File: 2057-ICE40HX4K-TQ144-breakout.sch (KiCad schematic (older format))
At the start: 41 parts, among them J1 Conn_02x30_Odd_Even, J2 Conn_02x30_Odd_Even, J3 RaspberryPI-B+header, J4 0548190519, J5 RaspberryPI-B+header, J6 Conn_02x06_Odd_Even, J7 Conn_02x01, U1 ICE40HX4K-TQ144, U2 AZ1117CH-3.3TRG1, U3 AZ1117CH-1.2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

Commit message: Added some ground vias, schematic PDF & some digikey nos.
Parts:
- C18, C20: Digi-Key_PN 1276-6455-1-ND -> 1276-1119-1-ND; MPN (none) -> CL10A106MQ8NNNC
- C19, C21: Digi-Key_PN 1276-6780-1-ND -> 1276-2868-1-ND; MPN (none) -> CL10A226MQ8NRNE
- C3, C5: Digi-Key_PN (none) -> 1276-1119-1-ND; MPN (none) -> CL10A106MQ8NNNC
- U1: Digi-Key_PN (none) -> 220-1572-ND; MPN (none) -> ICE40HX4K-TQ144
- U2: MPN (none) -> AZ1117CH-3.3TRG1
- U3: MPN (none) -> AZ1117CH-1.2TRG1
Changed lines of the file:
@@
 F 2 "Package_QFP:TQFP-144_20x20mm_P0.5mm" H 3100 1000 50  0001 R CNN
 F 3 "http://www.latticesemi.com/Products/FPGAandCPLD/iCE40" H 1100 5400 50  0001 C CNN
+F 4 "220-1572-ND" H 2100 2900 50  0001 C CNN "Digi-Key_PN"
+F 5 "ICE40HX4K-TQ144" H 2100 2900 50  0001 C CNN "MPN"
 	1    2100 2900
 	1    0    0    -1
@@
 F 2 "Package_QFP:TQFP-144_20x20mm_P0.5mm" H 5150 900 50  0001 R CNN
 F 3 "http://www.latticesemi.com/Products/FPGAandCPLD/iCE40" H 3150 5300 50  0001 C CNN
+F 4 "220-1572-ND" H 4150 2800 50  0001 C CNN "Digi-Key_PN"
+F 5 "ICE40HX4K-TQ144" H 4150 2800 50  0001 C CNN "MPN"
 	2    4150 2800
 	1    0    0    -1
@@
 F 2 "Package_QFP:TQFP-144_20x20mm_P0.5mm" H 8700 1400 50  0001 R CNN
 F 3 "http://www.latticesemi.com/Products/FPGAandCPLD/iCE40" H 6700 5800 50  0001 C CNN
+F 4 "220-1572-ND" H 7700 3300 50  0001 C CNN "Digi-Key_PN"
+F 5 "ICE40HX4K-TQ144" H 7700 3300 50  0001 C CNN "MPN"
 	3    7700 3300
 	1    0    0    -1
@@
 F 2 "Package_QFP:TQFP-144_20x20mm_P0.5mm" H 7050 900 50  0001 R CNN
 F 3 "http://www.latticesemi.com/Products/FPGAandCPLD/iCE40" H 5050 5300 50  0001 C CNN
+F 4 "220-1572-ND" H 6050 2800 50  0001 C CNN "Digi-Key_PN"
+F 5 "ICE40HX4K-TQ144" H 6050 2800 50  0001 C CNN "MPN"
 	4    6050 2800
 	1    0    0    -1
@@
 F 2 "Package_QFP:TQFP-144_20x20mm_P0.5mm" H 11150 850 50  0001 R CNN
 F 3 "http://www.latticesemi.com/Products/FPGAandCPLD/iCE40" H 9150 5250 50  0001 C CNN
+F 4 "220-1572-ND" H 10150 2750 50  0001 C CNN "Digi-Key_PN"
+F 5 "ICE40HX4K-TQ144" H 10150 2750 50  0001 C CNN "MPN"
 	5    10150 2750
 	1    0    0    -1
@@
 F 2 "Capacitor_SMD:C_0603_1608Metric_Pad1.05x0.95mm_HandSolder" H 12138 2050 50  0001 C CNN
 F 3 "~" H 12100 2200 50  0001 C CNN
+F 4 "1276-1119-1-ND" H 12100 2200 50  0001 C CNN "Digi-Key_PN"
+F 5 "CL10A106MQ8NNNC" H 12100 2200 50  0001 C CNN "MPN"
 	1    12100 2200
 	1    0    0    -1
@@
 F 2 "Capacitor_SMD:C_0603_1608Metric_Pad1.05x0.95mm_HandSolder" H 12138 1500 50  0001 C CNN
 F 3 "~" H 12100 1650 50  0001 C CNN
+F 4 "1276-1119-1-ND" H 12100 1650 50  0001 C CNN "Digi-Key_PN"
+F 5 "CL10A106MQ8NNNC" H 12100 1650 50  0001 C CNN "MPN"
 	1    12100 1650
 	1    0    0    -1
@@
 F 3 "https://www.diodes.com/assets/Datasheets/AZ1117.pdf" H 14850 1800 50  0001 C CNN
 F 4 "AZ1117CH-3.3TRG1DICT-ND" H 14850 1800 50  0001 C CNN "Digi-Key_PN"
+F 5 "AZ1117CH-3.3TRG1" H 14850 1800 50  0001 C CNN "MPN"
 	1    14850 1800
 	1    0    0    -1
@@
 F 2 "Capacitor_SMD:C_0603_1608Metric_Pad1.05x0.95mm_HandSolder" H 14288 1800 50  0001 C CNN
 F 3 "~" H 14250 1950 50  0001 C CNN
-F 4 "1276-6455-1-ND" H 14250 1950 50  0001 C CNN "Digi-Key_PN"
+F 4 "1276-1119-1-ND" H 14250 1950 50  0001 C CNN "Digi-Key_PN"
+F 5 "CL10A106MQ8NNNC" H 14250 1950 50  0001 C CNN "MPN"
 	1    14250 1950
 	1    0    0    -1
@@
 F 2 "Capacitor_SMD:C_0603_1608Metric_Pad1.05x0.95mm_HandSolder" H 15338 1800 50  0001 C CNN
 F 3 "~" H 15300 1950 50  0001 C CNN
-F 4 "1276-6780-1-ND" H 15300 1950 50  0001 C CNN "Digi-Key_PN"
+F 4 "1276-2868-1-ND" H 15300 1950 50  0001 C CNN "Digi-Key_PN"
+F 5 "CL10A226MQ8NRNE" H 15300 1950 50  0001 C CNN "MPN"
 	1    15300 1950
 	1    0    0    -1
@@
 F 3 "https://www.diodes.com/assets/Datasheets/AZ1117.pdf" H 14900 2650 50  0001 C CNN
 F 4 "AZ1117CH-1.2TRG1DICT-ND" H 14900 2650 50  0001 C CNN "Digi-Key_PN"
+F 5 "AZ1117CH-1.2TRG1" H 14900 2650 50  0001 C CNN "MPN"
 	1    14900 2650
 	1    0    0    -1
@@
 F 2 "Capacitor_SMD:C_0603_1608Metric_Pad1.05x0.95mm_HandSolder" H 14338 2650 50  0001 C CNN
 F 3 "~" H 14300 2800 50  0001 C CNN
-F 4 "1276-6455-1-ND" H 14300 2800 50  0001 C CNN "Digi-Key_PN"
+F 4 "1276-1119-1-ND" H 14300 2800 50  0001 C CNN "Digi-Key_PN"
+F 5 "CL10A106MQ8NNNC" H 14300 2800 50  0001 C CNN "MPN"
 	1    14300 2800
 	1    0    0    -1
@@
 F 2 "Capacitor_SMD:C_0603_1608Metric_Pad1.05x0.95mm_HandSolder" H 15388 2650 50  0001 C CNN
 F 3 "~" H 15350 2800 50  0001 C CNN
-F 4 "1276-6780-1-ND" H 15350 2800 50  0001 C CNN "Digi-Key_PN"
+F 4 "1276-2868-1-ND" H 15350 2800 50  0001 C CNN "Digi-Key_PN"
+F 5 "CL10A226MQ8NRNE" H 15350 2800 50  0001 C CNN "MPN"
 	1    15350 2800
 	1    0    0    -1

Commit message: Fix programming headers, add LEDs, cosmetic fixes.
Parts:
- removed J6: Conn_02x06_Odd_Even, Connector_PinHeader_2.54mm:PinHeader_2x06_P2.54mm_Vertical, symbol Connector_Generic:Conn_02x06_Odd_Even
- added D10, D2, D3, D4, D5, D6, D7, D8, D9: LED_ALT, LED_SMD:LED_0603_1608Metric_Pad1.05x0.95mm_HandSolder, symbol Device:LED_ALT
- added J6: Conn_02x07_Odd_Even, Connector_PinHeader_2.54mm:PinHeader_2x07_P2.54mm_Vertical, symbol Connector_Generic:Conn_02x07_Odd_Even
- added R10, R11, R12, R13, R14, R6, R7, R8, R9: 330, Resistor_SMD:R_0603_1608Metric_Pad1.05x0.95mm_HandSolder, symbol Device:R
- Y1: footprint digikey-footprints:Oscillator_XLH536025.000000I -> jb-footprint:Oscillator_XLH536025.000000I
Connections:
- wire segments 464 -> 503
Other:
- moved on the sheet: C10, C11, C12, C13, C14, C15, C16, C17, C22, C23, C6, C7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

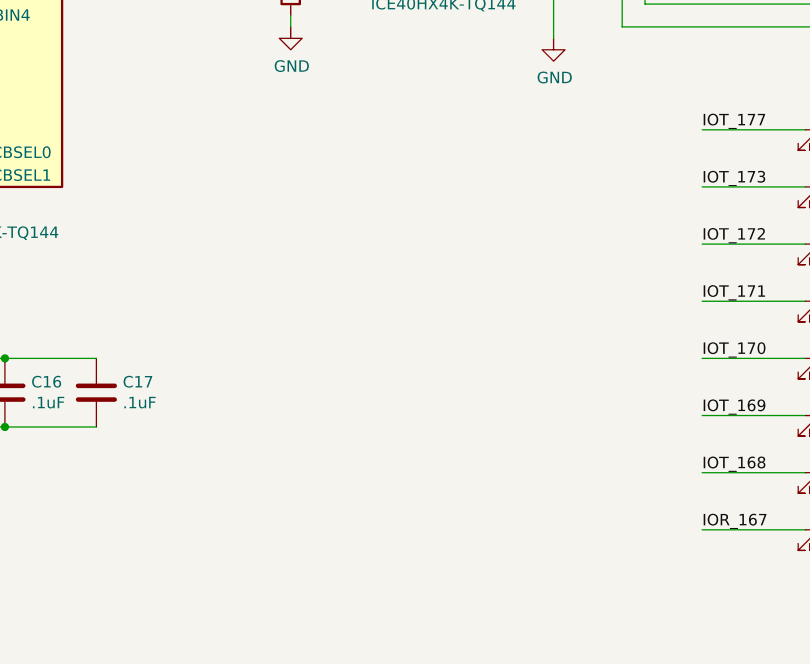
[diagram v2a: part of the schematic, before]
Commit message: Added two pushbuttons.
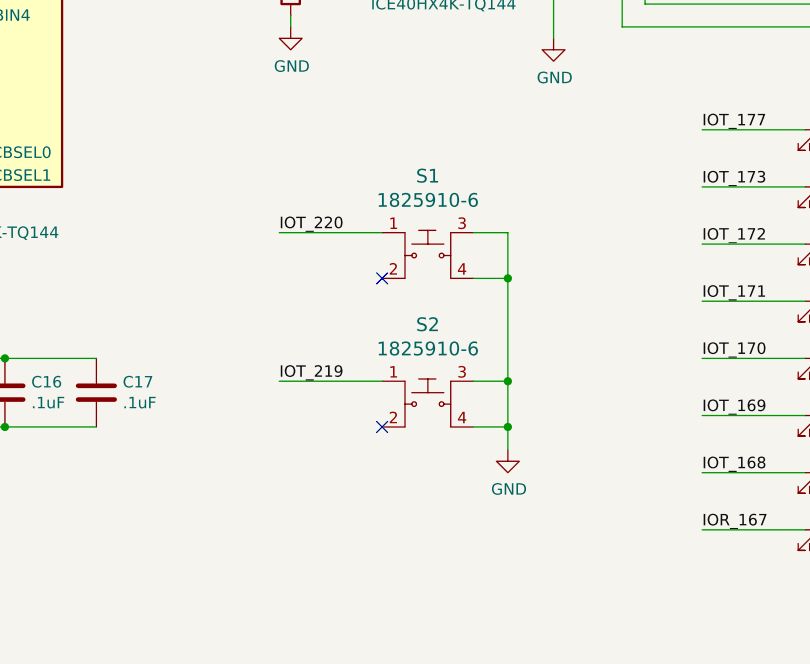
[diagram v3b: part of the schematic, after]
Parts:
- added S1, S2: 1825910-6, digikey-footprints:Switch_Tactile_THT_6x6mm, symbol dk_Tactile-Switches:1825910-6
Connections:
- net GND: now also S1.3, S1.4, S2.3, S2.4
- net IOT_219: now also S2.1
- net IOT_220: now also S1.1
- no-connect marks 5 -> 7
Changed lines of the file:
@@
 Text Label 10800 5850 0    50   ~ 0
 IOR_167
+$Comp
+L dk_Tactile-Switches:1825910-6 S1
+U 1 1 5E33EB87
+P 9600 4650
+F 0 "S1" H 9600 4997 60  0000 C CNN
+F 1 "1825910-6" H 9600 4891 60  0000 C CNN
+F 2 "digikey-footprints:Switch_Tactile_THT_6x6mm" H 9800 4850 60  0001 L CNN
+F 3 "https://www.te.com/commerce/DocumentDelivery/DDEController?Action=srchrtrv&DocNm=1825910&DocType=Customer+Drawing&DocLang=English" H 9800 4950 60  0001 L CNN
+F 4 "450-1650-ND" H 9800 5050 60  0001 L CNN "Digi-Key_PN"
+F 5 "1825910-6" H 9800 5150 60  0001 L CNN "MPN"
+F 6 "Switches" H 9800 5250 60  0001 L CNN "Category"
+F 7 "Tactile Switches" H 9800 5350 60  0001 L CNN "Family"
+F 8 "https://www.te.com/commerce/DocumentDelivery/DDEController?Action=srchrtrv&DocNm=1825910&DocType=Customer+Drawing&DocLang=English" H 9800 5450 60  0001 L CNN "DK_Datasheet_Link"
+F 9 "/product-detail/en/te-connectivity-alcoswitch-switches/1825910-6/450-1650-ND/1632536" H 9800 5550 60  0001 L CNN "DK_Detail_Page"
+F 10 "SWITCH TACTILE SPST-NO 0.05A 24V" H 9800 5650 60  0001 L CNN "Description"
+F 11 "TE Connectivity ALCOSWITCH Switches" H 9800 5750 60  0001 L CNN "Manufacturer"
+F 12 "Active" H 9800 5850 60  0001 L CNN "Status"
+	1    9600 4650
+	1    0    0    -1
+$EndComp
+$Comp
+L dk_Tactile-Switches:1825910-6 S2
+U 1 1 5E3405E8
+P 9600 5300
+F 0 "S2" H 9600 5647 60  0000 C CNN
+F 1 "1825910-6" H 9600 5541 60  0000 C CNN
+F 2 "digikey-footprints:Switch_Tactile_THT_6x6mm" H 9800 5500 60  0001 L CNN
+F 3 "https://www.te.com/commerce/DocumentDelivery/DDEController?Action=srchrtrv&DocNm=1825910&DocType=Customer+Drawing&DocLang=English" H 9800 5600 60  0001 L CNN
+F 4 "450-1650-ND" H 9800 5700 60  0001 L CNN "Digi-Key_PN"
+F 5 "1825910-6" H 9800 5800 60  0001 L CNN "MPN"
+F 6 "Switches" H 9800 5900 60  0001 L CNN "Category"
+F 7 "Tactile Switches" H 9800 6000 60  0001 L CNN "Family"
+F 8 "https://www.te.com/commerce/DocumentDelivery/DDEController?Action=srchrtrv&DocNm=1825910&DocType=Customer+Drawing&DocLang=English" H 9800 6100 60  0001 L CNN "DK_Datasheet_Link"
+F 9 "/product-detail/en/te-connectivity-alcoswitch-switches/1825910-6/450-1650-ND/1632536" H 9800 6200 60  0001 L CNN "DK_Detail_Page"
+F 10 "SWITCH TACTILE SPST-NO 0.05A 24V" H 9800 6300 60  0001 L CNN "Description"
+F 11 "TE Connectivity ALCOSWITCH Switches" H 9800 6400 60  0001 L CNN "Manufacturer"
+F 12 "Active" H 9800 6500 60  0001 L CNN "Status"
+	1    9600 5300
+	1    0    0    -1
+$EndComp
+$Comp
+L power:GND #PWR06
+U 1 1 5E341682
+P 9950 5500
+F 0 "#PWR06" H 9950 5250 50  0001 C CNN
+F 1 "GND" H 9955 5327 50  0000 C CNN
+F 2 "" H 9950 5500 50  0001 C CNN
+F 3 "" H 9950 5500 50  0001 C CNN
+	1    9950 5500
+	1    0    0    -1
+$EndComp
+Wire Wire Line
+	9800 4550 9950 4550
+Wire Wire Line
+	9950 4550 9950 4750
+Wire Wire Line
+	9800 5200 9950 5200
+Connection ~ 9950 5200
+Wire Wire Line
+	9950 5200 9950 5400
+Wire Wire Line
+	9800 5400 9950 5400
+Connection ~ 9950 5400
+Wire Wire Line
+	9950 5400 9950 5500
+Wire Wire Line
+	9800 4750 9950 4750
+Connection ~ 9950 4750
+Wire Wire Line
+	9950 4750 9950 5200
+Wire Wire Line
+	8950 4550 9400 4550
+Wire Wire Line
+	8950 5200 9400 5200
+NoConn ~ 9400 4750
+NoConn ~ 9400 5400
+Text Label 8950 4550 0    50   ~ 0
+IOT_220
+Text Label 8950 5200 0    50   ~ 0
+IOT_219
 $EndSCHEMATC

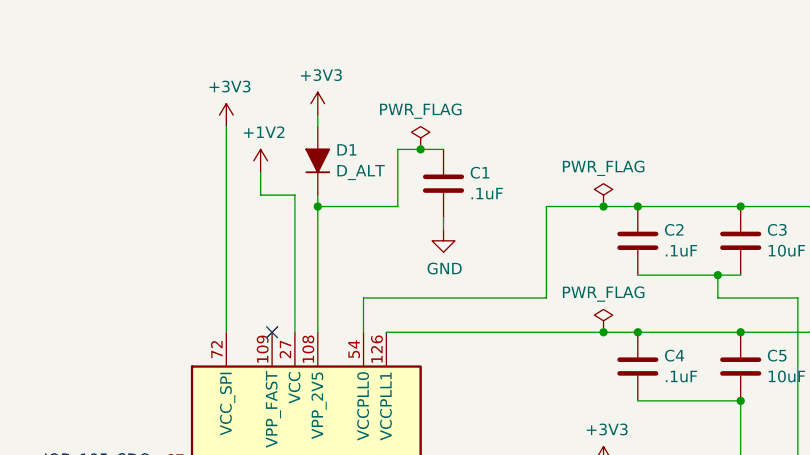
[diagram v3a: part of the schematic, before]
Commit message: Spec D1 as: 1N4448WSF-7 & label clock on pin 55
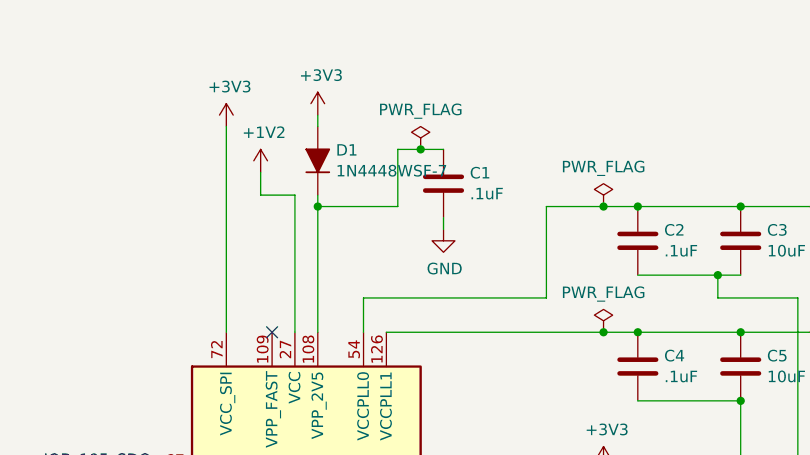
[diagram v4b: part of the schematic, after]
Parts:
- D1: value D_ALT -> 1N4448WSF-7
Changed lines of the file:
@@
 P 10250 1300
 F 0 "D1" V 10296 1221 50  0000 R CNN
-F 1 "D_ALT" V 10205 1221 50  0000 R CNN
+F 1 "1N4448WSF-7" V 10205 1221 50  0000 R CNN
 F 2 "Diode_SMD:D_0603_1608Metric_Pad1.05x0.95mm_HandSolder" H 10250 1300 50  0001 C CNN
 F 3 "~" H 10250 1300 50  0001 C CNN

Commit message: Add FLASH, SD, gnd testpoints for Rev 2.0
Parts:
- removed J6: Conn_02x07_Odd_Even, Connector_PinHeader_2.54mm:PinHeader_2x07_P2.54mm_Vertical, symbol Connector_Generic:Conn_02x07_Odd_Even
- added C24: .1uF, Capacitor_SMD:C_0603_1608Metric_Pad1.05x0.95mm_HandSolder, symbol Device:C
- added C25: 4.7uF, Capacitor_SMD:C_0603_1608Metric_Pad1.05x0.95mm_HandSolder, symbol Device:C
- added C26: .1uF, Capacitor_SMD:C_0603_1608Metric_Pad1.05x0.95mm_HandSolder, symbol Device:C_Small
- added D11, D12: 1N4448WSF-7, Diode_SMD:D_0603_1608Metric_Pad1.05x0.95mm_HandSolder, symbol Device:D_ALT
- added J6: Conn_02x08_Odd_Even, Connector_PinHeader_2.54mm:PinHeader_2x08_P2.54mm_Vertical, symbol Connector_Generic:Conn_02x08_Odd_Even
- added J8: Micro_SD_Card_Det, jb-footprint:microSD_HC_Hirose_DM3D-SF-bigpad, symbol Connector:Micro_SD_Card_Det
- added R15, R16: 10K, Resistor_SMD:R_0603_1608Metric_Pad1.05x0.95mm_HandSolder, symbol Device:R
- added TP1, TP2: RCW-0C, digikey-footprints:PROBE_PAD_1206, symbol dk_Test-Points:RCW-0C
- added U4: AT45DB161D-SU, digikey-footprints:SOIC-8_W5.6mm, symbol JWlib:AT45DB161D-SU
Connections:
- net +3V3: now also R5.2, C24.1, C25.1, C26.1, J8.4 (VDD), R15.2, R16.2, U4.5 (~WP~), U4.6 (Vcc)
- net CDONE: now also J6.2 (Pin_2)
- net GND: now also C24.2, C25.2, C26.2, J8.10 (DET_A), J8.11 (SHIELD), J8.6 (VSS), TP1.1, TP2.1, U4.7 (GND); no longer J2.5 (Pin_5), R5.1
- net GPIO12: now also J6.11 (Pin_11)
- net GPIO16: now also J6.15 (Pin_15)
- net GPIO23: now also J6.1 (Pin_1)
- net GPIO24: now also J6.3 (Pin_3)
- net IOB_105_SDO: now also J6.7 (Pin_7), U4.1 (SI)
- net IOB_106_SDI: now also J6.6 (Pin_6), U4.8 (SO)
- net IOB_107_SCK: now also J6.10 (Pin_10), R15.1, U4.2 (SCK)
- net IOB_108_SS: now also R5.1, D11.2 (A), D12.2 (A), U4.4 (~CS~); no longer R5.2
- net IOB_91: now also J2.5 (Pin_5)
- net IOT_206: now also J8.2 (DAT3/CD)
- net IOT_213: now also J8.3 (CMD)
- net IOT_215: now also J8.5 (CLK)
- net IOT_217: now also J8.7 (DAT0)
- net IOT_220: now also J8.9 (DET_B)
- net SPI_CE0: now also J6.13 (Pin_13)
- net SPI_MISO: now also J6.8 (Pin_8)
- net SPI_MOSI: now also J6.5 (Pin_5)
- net SPI_SCLK: now also J6.9 (Pin_9)
- net ~CRESET~: now also J6.4 (Pin_4)
- new net J6_CE0: D11.1 (K), J6.14 (Pin_14)
- new net J6_GPIO12: D12.1 (K), J6.12 (Pin_12)
- new net ~FRESET~: J6.16 (Pin_16), R16.1, U4.3 (~RESET~)
- no-connect marks 7 -> 9
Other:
- note added: "CLK"
- note added: "Copyright (C) 2019, 2023 John Winans\n\nThis documentation describes Open Hardware and is licensed under the CERN OHL v. 1.2.\n\nYou may redistribute and modify this documentation under the terms of the CERN OHL v.1.2. (http://ohwr.org/cernohl). \nThis documentation is distributed WITHOUT ANY EXPRESS OR IMPLIED WARRANTY, INCLUDING OF MERCHANTABILITY, \nSATISFACTORY QUALITY AND FITNESS FOR A PARTI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"
- note added: "DET"
- note added: "FLASH"
- note added: "FPGA"
- note added: "MISO"
- note added: "MISO/MOSI\nTarget Options"
- note added: "MOSI"
- note added: "SS low = SPI slave config\nSS high = SPI master config\n(SS has an internal pullup)"
- note added: "SSEL"
- note added: "https://github.com/johnwinans/2057-ICE40HX4K-TQ144-breakout"
- note removed: "Copyright (C) 2019 John Winans\n\nThis documentation describes Open Hardware and is licensed under the CERN OHL v. 1.2.\n\nYou may redistribute and modify this documentation under the terms of the CERN OHL v.1.2. (http://ohwr.org/cernohl). \nThis documentation is distributed WITHOUT ANY EXPRESS OR IMPLIED WARRANTY, INCLUDING OF MERCHANTABILITY, \nSATISFACTORY QUALITY AND FITNESS FOR A PARTICULAR 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"
- note removed: "https://github.com/johnwinans/2057-ICE40HX4K-TQ144-breakout.git"
- moved on the sheet: C10, C11, C12, C13, C14, C15, C16, C17, C22, C23, C6, C7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

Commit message: Change filter caps to 0805 Silk correct GPIO18 Silk mark GPIO12 Added C27
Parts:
- added C27: 22uF, Capacitor_SMD:C_0805_2012Metric_Pad1.15x1.40mm_HandSolder, symbol Device:C_Small
- C18, C19, C20, C21, C26: footprint Capacitor_SMD:C_0603_1608Metric_Pad1.05x0.95mm_HandSolder -> Capacitor_SMD:C_0805_2012Metric_Pad1.15x1.40mm_HandSolder
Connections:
- net +3V3: now also C27.1
- net GND: now also C27.2
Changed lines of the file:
@@
 Sheet 1 1
 Title "2057-ICE40HX4K-TQ144-breakout"
-Date "2023-04-29"
-Rev "2.0"
+Date "2023-05-13"
+Rev "2.1"
 Comp ""
 Comment1 ""
@@
 F 0 "C18" H 14365 2041 50  0000 L CNN
 F 1 "10uF" H 14365 1950 50  0000 L CNN
-F 2 "Capacitor_SMD:C_0603_1608Metric_Pad1.05x0.95mm_HandSolder" H 14288 1800 50  0001 C CNN
+F 2 "Capacitor_SMD:C_0805_2012Metric_Pad1.15x1.40mm_HandSolder" H 14288 1800 50  0001 C CNN
 F 3 "~" H 14250 1950 50  0001 C CNN
 F 4 "1276-1119-1-ND" H 14250 1950 50  0001 C CNN "Digi-Key_PN"
@@
 F 0 "C19" H 15415 2041 50  0000 L CNN
 F 1 "22uF" H 15415 1950 50  0000 L CNN
-F 2 "Capacitor_SMD:C_0603_1608Metric_Pad1.05x0.95mm_HandSolder" H 15338 1800 50  0001 C CNN
+F 2 "Capacitor_SMD:C_0805_2012Metric_Pad1.15x1.40mm_HandSolder" H 15338 1800 50  0001 C CNN
 F 3 "~" H 15300 1950 50  0001 C CNN
 F 4 "1276-2868-1-ND" H 15300 1950 50  0001 C CNN "Digi-Key_PN"
@@
 F 0 "C20" H 14415 2891 50  0000 L CNN
 F 1 "10uF" H 14415 2800 50  0000 L CNN
-F 2 "Capacitor_SMD:C_0603_1608Metric_Pad1.05x0.95mm_HandSolder" H 14338 2650 50  0001 C CNN
+F 2 "Capacitor_SMD:C_0805_2012Metric_Pad1.15x1.40mm_HandSolder" H 14338 2650 50  0001 C CNN
 F 3 "~" H 14300 2800 50  0001 C CNN
 F 4 "1276-1119-1-ND" H 14300 2800 50  0001 C CNN "Digi-Key_PN"
@@
 F 0 "C21" H 15465 2891 50  0000 L CNN
 F 1 "22uF" H 15465 2800 50  0000 L CNN
-F 2 "Capacitor_SMD:C_0603_1608Metric_Pad1.05x0.95mm_HandSolder" H 15388 2650 50  0001 C CNN
+F 2 "Capacitor_SMD:C_0805_2012Metric_Pad1.15x1.40mm_HandSolder" H 15388 2650 50  0001 C CNN
 F 3 "~" H 15350 2800 50  0001 C CNN
 F 4 "1276-2868-1-ND" H 15350 2800 50  0001 C CNN "Digi-Key_PN"
@@
 $EndComp
 Wire Wire Line
-	5250 6550 5250 6850
+	5250 6550 5250 6650
 Wire Wire Line
 	5250 6550 6200 6550
@@
 F 0 "C26" H 5342 6496 50  0000 L CNN
 F 1 ".1uF" H 5342 6405 50  0000 L CNN
-F 2 "Capacitor_SMD:C_0603_1608Metric_Pad1.05x0.95mm_HandSolder" H 5250 6450 50  0001 C CNN
+F 2 "Capacitor_SMD:C_0805_2012Metric_Pad1.15x1.40mm_HandSolder" H 5250 6450 50  0001 C CNN
 F 3 "~" H 5250 6450 50  0001 C CNN
 	1    5250 6450
@@
 	5250 6350 6200 6350
 Wire Wire Line
-	5250 6350 5250 5950
+	5250 6350 5250 6250
 Connection ~ 5250 6350
 $Comp
@@
 	-1   0    0    1
 $EndComp
+$Comp
+L Device:C_Small C27
+U 1 1 646EB4DF
+P 4900 6450
+F 0 "C27" H 4992 6496 50  0000 L CNN
+F 1 "22uF" H 4992 6405 50  0000 L CNN
+F 2 "Capacitor_SMD:C_0805_2012Metric_Pad1.15x1.40mm_HandSolder" H 4900 6450 50  0001 C CNN
+F 3 "~" H 4900 6450 50  0001 C CNN
+F 4 "1276-2868-1-ND" H 4900 6450 50  0001 C CNN "Digi-Key_PN"
+F 5 "CL10A226MQ8NRNE" H 4900 6450 50  0001 C CNN "MPN"
+	1    4900 6450
+	1    0    0    -1
+$EndComp
+Wire Wire Line
+	4900 6350 4900 6250
+Wire Wire Line
+	4900 6250 5250 6250
+Connection ~ 5250 6250
+Wire Wire Line
+	5250 6250 5250 5950
+Wire Wire Line
+	4900 6550 4900 6650
+Wire Wire Line
+	4900 6650 5250 6650
+Connection ~ 5250 6650
+Wire Wire Line
+	5250 6650 5250 6850
 $EndSCHEMATC
